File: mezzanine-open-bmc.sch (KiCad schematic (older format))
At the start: 4 parts, among them P1 CONN_02X20, P2 CONN_02X20, SW1 PWR, SW2 RST

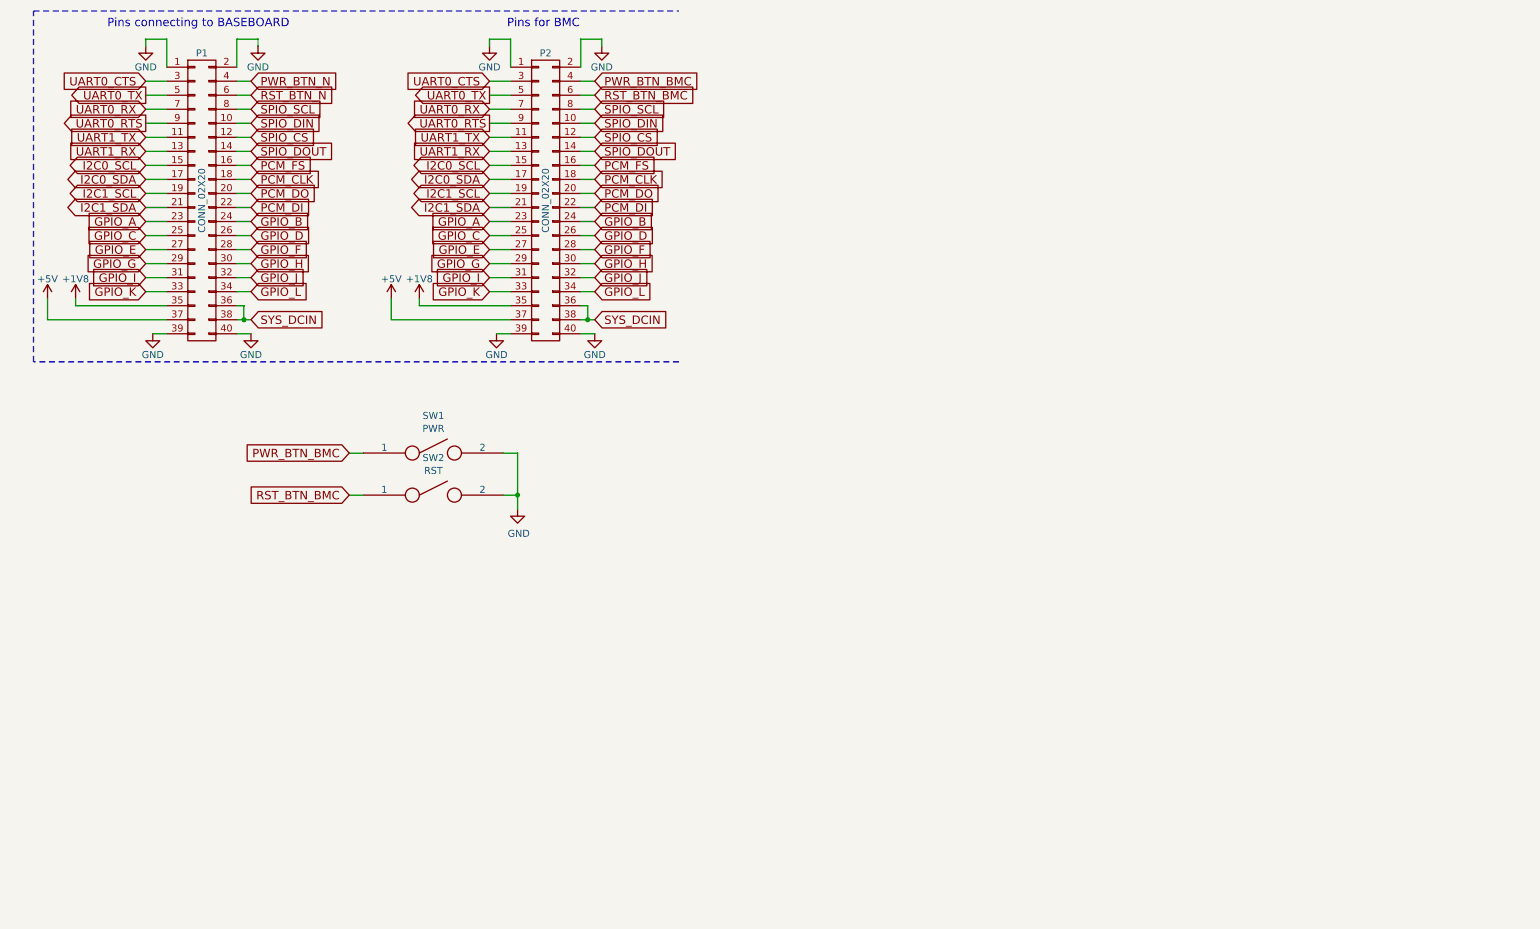
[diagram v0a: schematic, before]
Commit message: Connect BB UART1 to BMC UART1
All pins on the BMC header pins now have "_BMC" appended to their signal
names. This is to allow connections to be made from different pins on the
BB (Baseboard).
UART1 on the BB is now connected to UART1 on the BMC

Signed-off-by: Sophie Haynes <sophie.haynes@linaro.org>
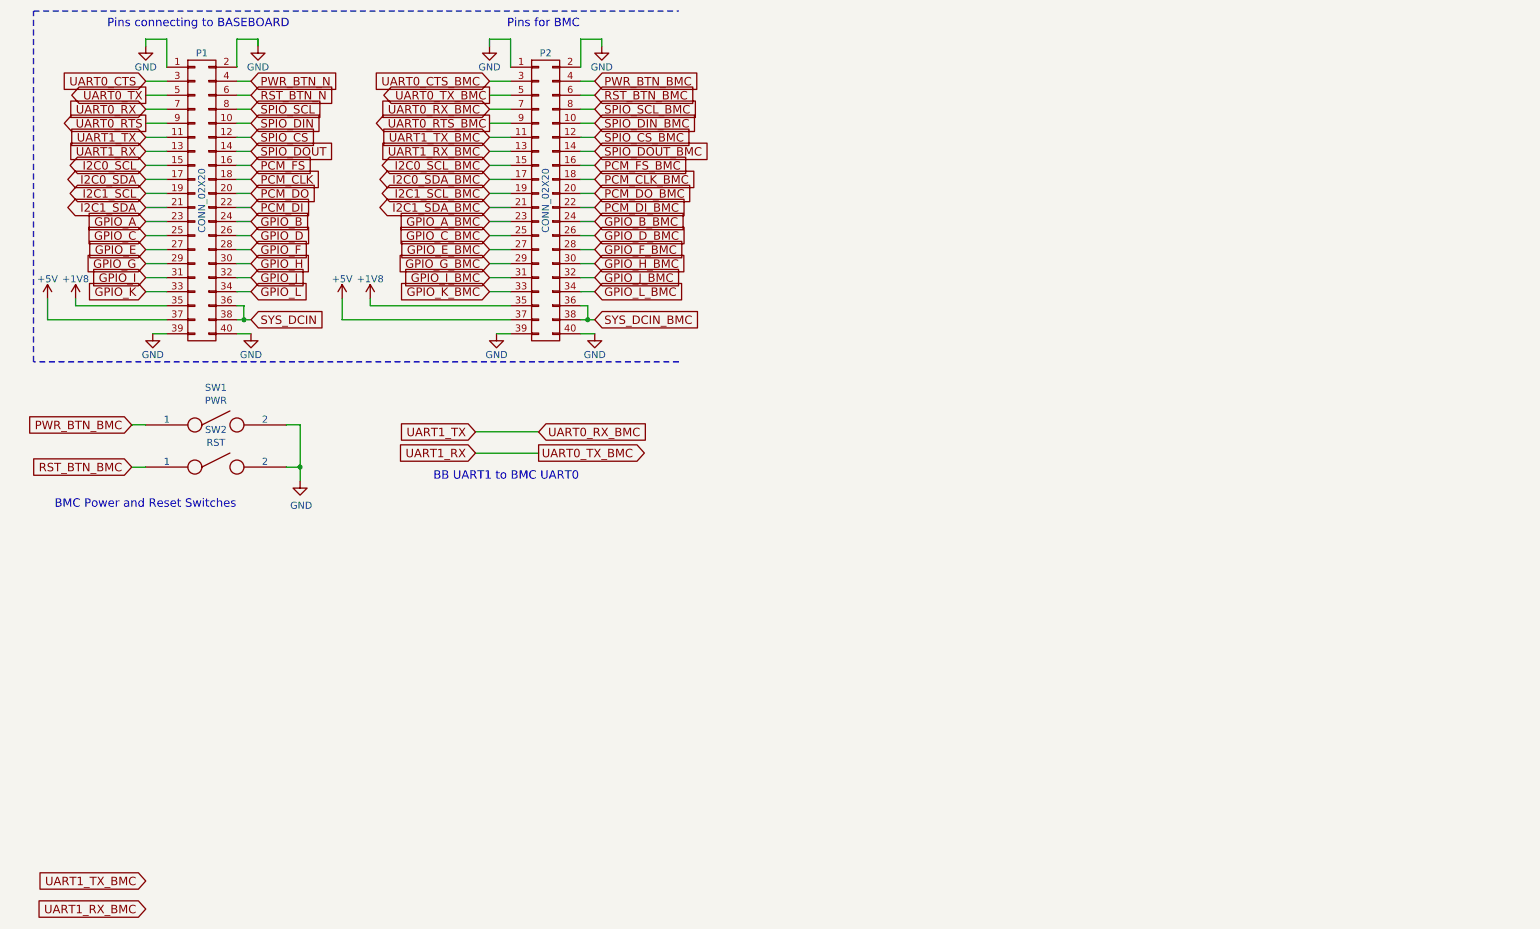
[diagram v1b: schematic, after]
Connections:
- net GPIO_A: no longer P2.23 (P23)
- net GPIO_B: no longer P2.24 (P24)
- net GPIO_C: no longer P2.25 (P25)
- net GPIO_D: no longer P2.26 (P26)
- net GPIO_E: no longer P2.27 (P27)
- net GPIO_F: no longer P2.28 (P28)
- net GPIO_G: no longer P2.29 (P29)
- net GPIO_H: no longer P2.30 (P30)
- net GPIO_I: no longer P2.31 (P31)
- net GPIO_J: no longer P2.32 (P32)
- net GPIO_K: no longer P2.33 (P33)
- net GPIO_L: no longer P2.34 (P34)
- net I2C0_SCL: no longer P2.15 (P15)
- net I2C0_SDA: no longer P2.17 (P17)
- net I2C1_SCL: no longer P2.19 (P19)
- net I2C1_SDA: no longer P2.21 (P21)
- net PCM_CLK: no longer P2.18 (P18)
- net PCM_DI: no longer P2.22 (P22)
- net PCM_DO: no longer P2.20 (P20)
- net PCM_FS: no longer P2.16 (P16)
- net SPIO_CS: no longer P2.12 (P12)
- net SPIO_DIN: no longer P2.10 (P10)
- net SPIO_DOUT: no longer P2.14 (P14)
- net SPIO_SCL: no longer P2.8 (P8)
- net SYS_DCIN: no longer P2.36 (P36), P2.38 (P38)
- net UART0_CTS: no longer P2.3 (P3)
- net UART0_RTS: no longer P2.9 (P9)
- net UART0_RX: no longer P2.7 (P7)
- net UART0_TX: no longer P2.5 (P5)
- net UART1_RX renamed UART0_TX_BMC
- net UART0_TX_BMC: now also P2.5 (P5); no longer P2.13 (P13)
- net UART1_TX renamed UART0_RX_BMC
- net UART0_RX_BMC: now also P2.7 (P7); no longer P2.11 (P11)
- new net GPIO_A_BMC: P2.23 (P23)
- new net GPIO_B_BMC: P2.24 (P24)
- new net GPIO_C_BMC: P2.25 (P25)
- new net GPIO_D_BMC: P2.26 (P26)
- new net GPIO_E_BMC: P2.27 (P27)
- new net GPIO_F_BMC: P2.28 (P28)
- new net GPIO_G_BMC: P2.29 (P29)
- new net GPIO_H_BMC: P2.30 (P30)
- new net GPIO_I_BMC: P2.31 (P31)
- new net GPIO_J_BMC: P2.32 (P32)
- new net GPIO_K_BMC: P2.33 (P33)
- new net GPIO_L_BMC: P2.34 (P34)
- new net I2C0_SCL_BMC: P2.15 (P15)
- new net I2C0_SDA_BMC: P2.17 (P17)
- new net I2C1_SCL_BMC: P2.19 (P19)
- new net I2C1_SDA_BMC: P2.21 (P21)
- new net PCM_CLK_BMC: P2.18 (P18)
- new net PCM_DI_BMC: P2.22 (P22)
- new net PCM_DO_BMC: P2.20 (P20)
- new net PCM_FS_BMC: P2.16 (P16)
- new net SPIO_CS_BMC: P2.12 (P12)
- new net SPIO_DIN_BMC: P2.10 (P10)
- new net SPIO_DOUT_BMC: P2.14 (P14)
- new net SPIO_SCL_BMC: P2.8 (P8)
- new net SYS_DCIN_BMC: P2.36 (P36), P2.38 (P38)
- new net UART0_CTS_BMC: P2.3 (P3)
- new net UART0_RTS_BMC: P2.9 (P9)
- new net UART1_RX_BMC: P2.13 (P13)
- new net UART1_TX_BMC: P2.11 (P11)
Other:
- note added: "BB UART1 to BMC UART0"
- note added: "BMC Power and Reset Switches"
- moved on the sheet: SW1, SW2
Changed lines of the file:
@@
 $EndDescr
 Text GLabel 3950 1500 0    60   Output ~ 0
-UART0_RTS
+UART0_RTS_BMC
 $Comp
 L GND #PWR9
@@
 $EndComp
 Text GLabel 3950 1300 0    60   Output ~ 0
-UART0_TX
+UART0_TX_BMC
 $Comp
 L GND #PWR10
@@
 $EndComp
 Text GLabel 3950 1200 0    60   Input ~ 0
-UART0_CTS
+UART0_CTS_BMC
 Text GLabel 4700 2900 2    60   Input ~ 0
-SYS_DCIN
+SYS_DCIN_BMC
 $Comp
 L GND #PWR13
@@
 L +1V8 #PWR8
 U 1 1 55D4822C
-P 3450 2750
-F 0 "#PWR8" H 3450 2600 50  0001 C CNN
-F 1 "+1V8" H 3450 2890 50  0000 C CNN
-F 2 "" H 3450 2750 60  0000 C CNN
-F 3 "" H 3450 2750 60  0000 C CNN
-	1    3450 2750
+P 3100 2750
+F 0 "#PWR8" H 3100 2600 50  0001 C CNN
+F 1 "+1V8" H 3100 2890 50  0000 C CNN
+F 2 "" H 3100 2750 60  0000 C CNN
+F 3 "" H 3100 2750 60  0000 C CNN
+	1    3100 2750
 	1    0    0    -1
 $EndComp
@@
 L +5V #PWR7
 U 1 1 55D48233
-P 3250 2750
-F 0 "#PWR7" H 3250 2600 50  0001 C CNN
-F 1 "+5V" H 3250 2890 50  0000 C CNN
-F 2 "" H 3250 2750 60  0000 C CNN
-F 3 "" H 3250 2750 60  0000 C CNN
-	1    3250 2750
+P 2900 2750
+F 0 "#PWR7" H 2900 2600 50  0001 C CNN
+F 1 "+5V" H 2900 2890 50  0000 C CNN
+F 2 "" H 2900 2750 60  0000 C CNN
+F 3 "" H 2900 2750 60  0000 C CNN
+	1    2900 2750
 	1    0    0    -1
 $EndComp
@@
 RST_BTN_BMC
 Text GLabel 3950 2100 0    60   BiDi ~ 0
-I2C1_SDA
+I2C1_SDA_BMC
 Text GLabel 3950 2000 0    60   BiDi ~ 0
-I2C1_SCL
+I2C1_SCL_BMC
 Text GLabel 3950 1900 0    60   BiDi ~ 0
-I2C0_SDA
+I2C0_SDA_BMC
 Text GLabel 3950 1800 0    60   BiDi ~ 0
-I2C0_SCL
+I2C0_SCL_BMC
 Text GLabel 3950 2200 0    60   Input ~ 0
-GPIO_A
+GPIO_A_BMC
 Text GLabel 3950 1400 0    60   Input ~ 0
-UART0_RX
+UART0_RX_BMC
 Text GLabel 4700 1200 2    60   Input ~ 0
 PWR_BTN_BMC
 Text GLabel 3950 1600 0    60   Input ~ 0
-UART1_TX
+UART1_TX_BMC
 Text GLabel 3950 2300 0    60   Input ~ 0
-GPIO_C
+GPIO_C_BMC
 Text GLabel 3950 2400 0    60   Input ~ 0
-GPIO_E
+GPIO_E_BMC
 Text GLabel 3950 2500 0    60   Input ~ 0
-GPIO_G
+GPIO_G_BMC
 Text GLabel 3950 2600 0    60   Input ~ 0
-GPIO_I
+GPIO_I_BMC
 Text GLabel 3950 2700 0    60   Input ~ 0
-GPIO_K
+GPIO_K_BMC
 Text GLabel 3950 1700 0    60   Input ~ 0
-UART1_RX
+UART1_RX_BMC
 Text GLabel 4700 2200 2    60   Input ~ 0
-GPIO_B
+GPIO_B_BMC
 Text GLabel 4700 1400 2    60   Input ~ 0
-SPIO_SCL
+SPIO_SCL_BMC
 Text GLabel 4700 1500 2    60   Input ~ 0
-SPIO_DIN
+SPIO_DIN_BMC
 Text GLabel 4700 1600 2    60   Input ~ 0
-SPIO_CS
+SPIO_CS_BMC
 Text GLabel 4700 1700 2    60   Input ~ 0
-SPIO_DOUT
+SPIO_DOUT_BMC
 Text GLabel 4700 1800 2    60   Input ~ 0
-PCM_FS
+PCM_FS_BMC
 Text GLabel 4700 1900 2    60   Input ~ 0
-PCM_CLK
+PCM_CLK_BMC
 Text GLabel 4700 2000 2    60   Input ~ 0
-PCM_DO
+PCM_DO_BMC
 Text GLabel 4700 2100 2    60   Input ~ 0
-PCM_DI
+PCM_DI_BMC
 Text GLabel 4700 2300 2    60   Input ~ 0
-GPIO_D
+GPIO_D_BMC
 Text GLabel 4700 2400 2    60   Input ~ 0
-GPIO_F
+GPIO_F_BMC
 Text GLabel 4700 2500 2    60   Input ~ 0
-GPIO_H
+GPIO_H_BMC
 Text GLabel 4700 2600 2    60   Input ~ 0
-GPIO_J
+GPIO_J_BMC
 Text GLabel 4700 2700 2    60   Input ~ 0
-GPIO_L
+GPIO_L_BMC
 Wire Wire Line
 	4600 1200 4700 1200
@@
 	4750 900  4750 950
 Wire Wire Line
-	3250 2750 3250 2900
-Wire Wire Line
-	3450 2750 3450 2800
-Wire Wire Line
 	3950 2400 4100 2400
 Wire Wire Line
@@
 Wire Wire Line
 	3950 2700 4100 2700
-Wire Wire Line
-	3450 2800 4100 2800
 Wire Wire Line
 	4100 900  4100 1100
@@
 Wire Wire Line
 	4600 3000 4700 3000
-Wire Wire Line
-	3250 2900 4100 2900
 Wire Wire Line
 	3950 1300 4100 1300
@@
 Wire Notes Line
 	700  700  5300 700
-Text GLabel 2950 4150 0    60   Input ~ 0
+Text GLabel 1400 3950 0    60   Input ~ 0
 RST_BTN_BMC
-Text GLabel 2950 3850 0    60   Input ~ 0
+Text GLabel 1400 3650 0    60   Input ~ 0
 PWR_BTN_BMC
 $Comp
 L SPST SW1
 U 1 1 56D59D87
-P 3550 3850
-F 0 "SW1" H 3550 4116 50  0000 C CNN
-F 1 "PWR" H 3550 4024 50  0000 C CNN
-F 2 "" H 3550 3850 50  0000 C CNN
-F 3 "" H 3550 3850 50  0000 C CNN
-	1    3550 3850
+P 2000 3650
+F 0 "SW1" H 2000 3916 50  0000 C CNN
+F 1 "PWR" H 2000 3824 50  0000 C CNN
+F 2 "" H 2000 3650 50  0000 C CNN
+F 3 "" H 2000 3650 50  0000 C CNN
+	1    2000 3650
 	1    0    0    -1
 $EndComp
@@
 L SPST SW2
 U 1 1 56D59DC4
-P 3550 4150
-F 0 "SW2" H 3550 4416 50  0000 C CNN
-F 1 "RST" H 3550 4324 50  0000 C CNN
-F 2 "" H 3550 4150 50  0000 C CNN
-F 3 "" H 3550 4150 50  0000 C CNN
-	1    3550 4150
-	1    0    0    -1
-$EndComp
-Wire Wire Line
-	2950 3850 3050 3850
-Wire Wire Line
-	2950 4150 3050 4150
+P 2000 3950
+F 0 "SW2" H 2000 4216 50  0000 C CNN
+F 1 "RST" H 2000 4124 50  0000 C CNN
+F 2 "" H 2000 3950 50  0000 C CNN
+F 3 "" H 2000 3950 50  0000 C CNN
+	1    2000 3950
+	1    0    0    -1
+$EndComp
+Wire Wire Line
+	1400 3650 1500 3650
+Wire Wire Line
+	1400 3950 1500 3950
 $Comp
 L GND #PWR11
 U 1 1 56D59F1C
-P 4150 4250
-F 0 "#PWR11" H 4150 4000 50  0001 C CNN
-F 1 "GND" H 4158 4076 50  0000 C CNN
-F 2 "" H 4150 4250 50  0000 C CNN
-F 3 "" H 4150 4250 50  0000 C CNN
-	1    4150 4250
-	1    0    0    -1
-$EndComp
-Wire Wire Line
-	4150 4250 4150 3850
-Wire Wire Line
-	4150 3850 4050 3850
-Wire Wire Line
-	4050 4150 4150 4150
-Connection ~ 4150 4150
+P 2600 4050
+F 0 "#PWR11" H 2600 3800 50  0001 C CNN
+F 1 "GND" H 2608 3876 50  0000 C CNN
+F 2 "" H 2600 4050 50  0000 C CNN
+F 3 "" H 2600 4050 50  0000 C CNN
+	1    2600 4050
+	1    0    0    -1
+$EndComp
+Wire Wire Line
+	2600 3650 2600 4050
+Wire Wire Line
+	2600 3650 2500 3650
+Wire Wire Line
+	2500 3950 2600 3950
+Connection ~ 2600 3950
+Wire Wire Line
+	4100 2800 3100 2800
+Wire Wire Line
+	3100 2800 3100 2750
+Wire Wire Line
+	4100 2900 2900 2900
+Wire Wire Line
+	2900 2900 2900 2750
+Text GLabel 1500 6900 0    60   Input ~ 0
+UART1_TX_BMC
+Text GLabel 1500 7100 0    60   Input ~ 0
+UART1_RX_BMC
+Text GLabel 4300 3850 2    60   Output ~ 0
+UART0_TX_BMC
+Text GLabel 4300 3700 2    60   Input ~ 0
+UART0_RX_BMC
+Text GLabel 3850 3700 0    60   Input ~ 0
+UART1_TX
+Text GLabel 3850 3850 0    60   Input ~ 0
+UART1_RX
+Wire Wire Line
+	3850 3700 4300 3700
+Wire Wire Line
+	3850 3850 4300 3850
+Text Notes 850  4250 0    60   ~ 0
+BMC Power and Reset Switches
+Text Notes 3550 4050 0    60   ~ 0
+BB UART1 to BMC UART0
 $EndSCHEMATC

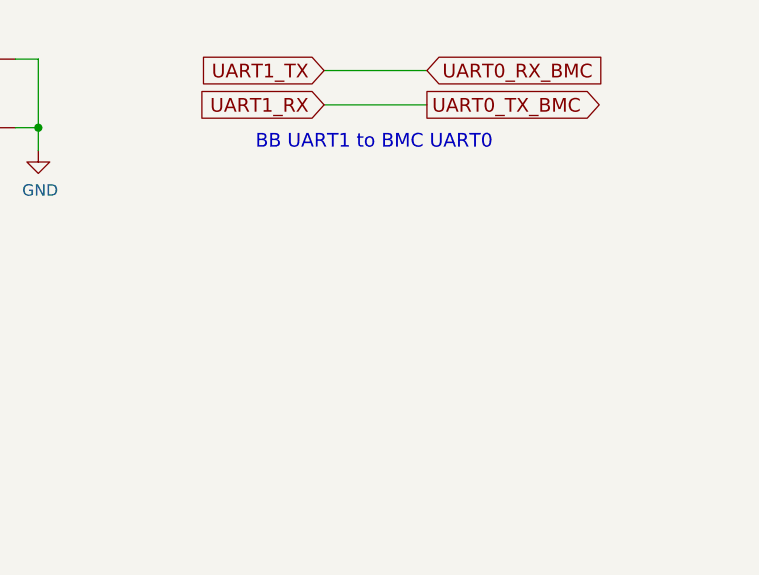
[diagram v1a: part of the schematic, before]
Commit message: Connect BB GPIO_A/B to BMC GPIO_A/B
GPIO A & B are now connected on the BB to the BMC.

Signed-off-by: Sophie Haynes <sophie.haynes@linaro.org>
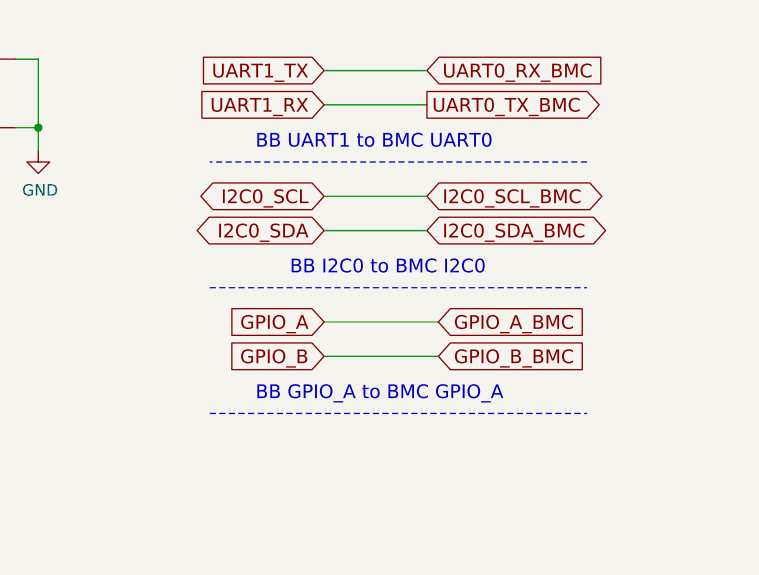
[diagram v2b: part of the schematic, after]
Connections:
- net GPIO_A_BMC is gone; now on net GPIO_A: P2.23 (P23)
- net GPIO_B_BMC is gone; now on net GPIO_B: P2.24 (P24)
- net I2C0_SCL_BMC is gone; now on net I2C0_SCL: P2.15 (P15)
- net I2C0_SDA_BMC is gone; now on net I2C0_SDA: P2.17 (P17)
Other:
- note added: "BB GPIO_A to BMC GPIO_A"
- note added: "BB I2C0 to BMC I2C0"
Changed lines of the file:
@@
 Text Notes 3550 4050 0    60   ~ 0
 BB UART1 to BMC UART0
+Text GLabel 3850 4400 0    60   BiDi ~ 0
+I2C0_SDA
+Text GLabel 3850 4250 0    60   BiDi ~ 0
+I2C0_SCL
+Text GLabel 4300 4400 2    60   BiDi ~ 0
+I2C0_SDA_BMC
+Text GLabel 4300 4250 2    60   BiDi ~ 0
+I2C0_SCL_BMC
+Wire Wire Line
+	3850 4250 4300 4250
+Wire Wire Line
+	4300 4400 3850 4400
+Wire Notes Line
+	5000 4100 3350 4100
+Text Notes 3700 4600 0    60   ~ 0
+BB I2C0 to BMC I2C0
+Text GLabel 3850 4800 0    60   Input ~ 0
+GPIO_A
+Text GLabel 3850 4950 0    60   Input ~ 0
+GPIO_B
+Text GLabel 4350 4800 2    60   Input ~ 0
+GPIO_A_BMC
+Text GLabel 4350 4950 2    60   Input ~ 0
+GPIO_B_BMC
+Wire Wire Line
+	3850 4800 4350 4800
+Wire Wire Line
+	4350 4950 3850 4950
+Wire Notes Line
+	3350 4650 5000 4650
+Text Notes 3550 5150 0    60   ~ 0
+BB GPIO_A to BMC GPIO_A
+Wire Notes Line
+	3350 5200 5000 5200
 $EndSCHEMATC

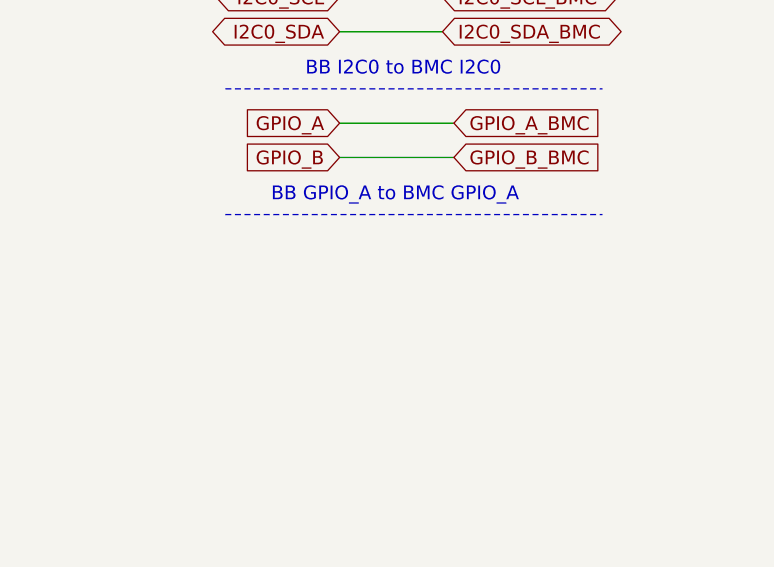
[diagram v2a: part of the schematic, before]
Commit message: Connect BB PWR/RST to BMC GPIO
The BB PWR BTN is now wired to BMC GPIO C.
BB RST BTN is wired to BMC GPIO D.

Signed-off-by: Sophie Haynes <osphie.haynes@linaro.org>
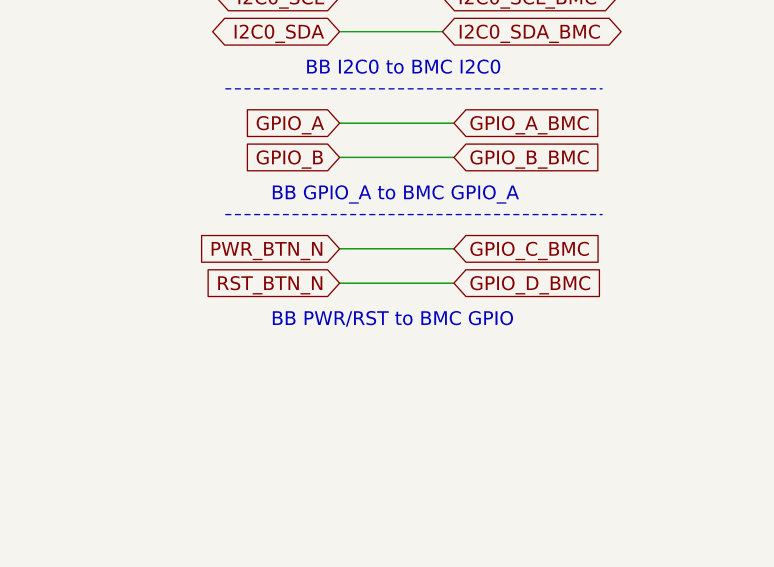
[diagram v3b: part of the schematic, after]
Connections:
- net PWR_BTN_N is gone; now on net GPIO_C_BMC: P1.4 (P4)
- net RST_BTN_N is gone; now on net GPIO_D_BMC: P1.6 (P6)
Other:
- note added: "BB PWR/RST to BMC GPIO"
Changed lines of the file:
@@
 Wire Notes Line
 	3350 5200 5000 5200
+Text GLabel 4350 5350 2    60   Input ~ 0
+GPIO_C_BMC
+Text GLabel 3850 5350 0    60   Input ~ 0
+PWR_BTN_N
+Text GLabel 3850 5500 0    60   Input ~ 0
+RST_BTN_N
+Text GLabel 4350 5500 2    60   Input ~ 0
+GPIO_D_BMC
+Wire Wire Line
+	4350 5350 3850 5350
+Wire Wire Line
+	3850 5500 4350 5500
+Text Notes 3550 5700 0    60   ~ 0
+BB PWR/RST to BMC GPIO
 $EndSCHEMATC
